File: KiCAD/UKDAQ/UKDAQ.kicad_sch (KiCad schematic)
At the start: 20 parts

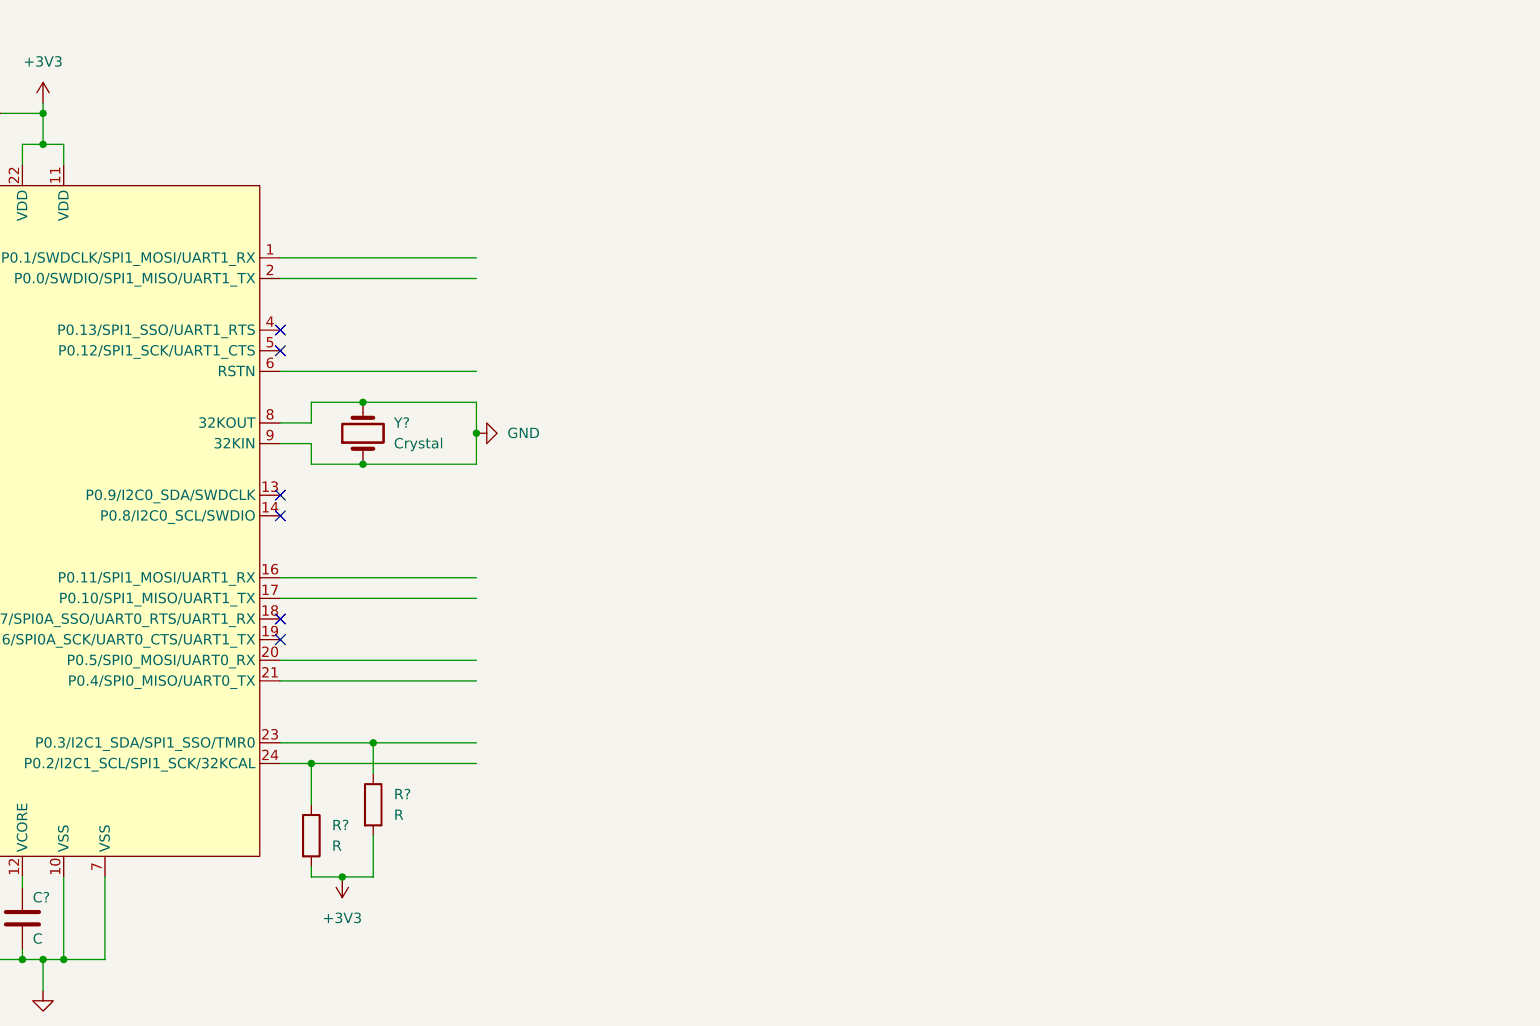
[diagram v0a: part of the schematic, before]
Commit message: created eclipse IDE workspace for dev kit
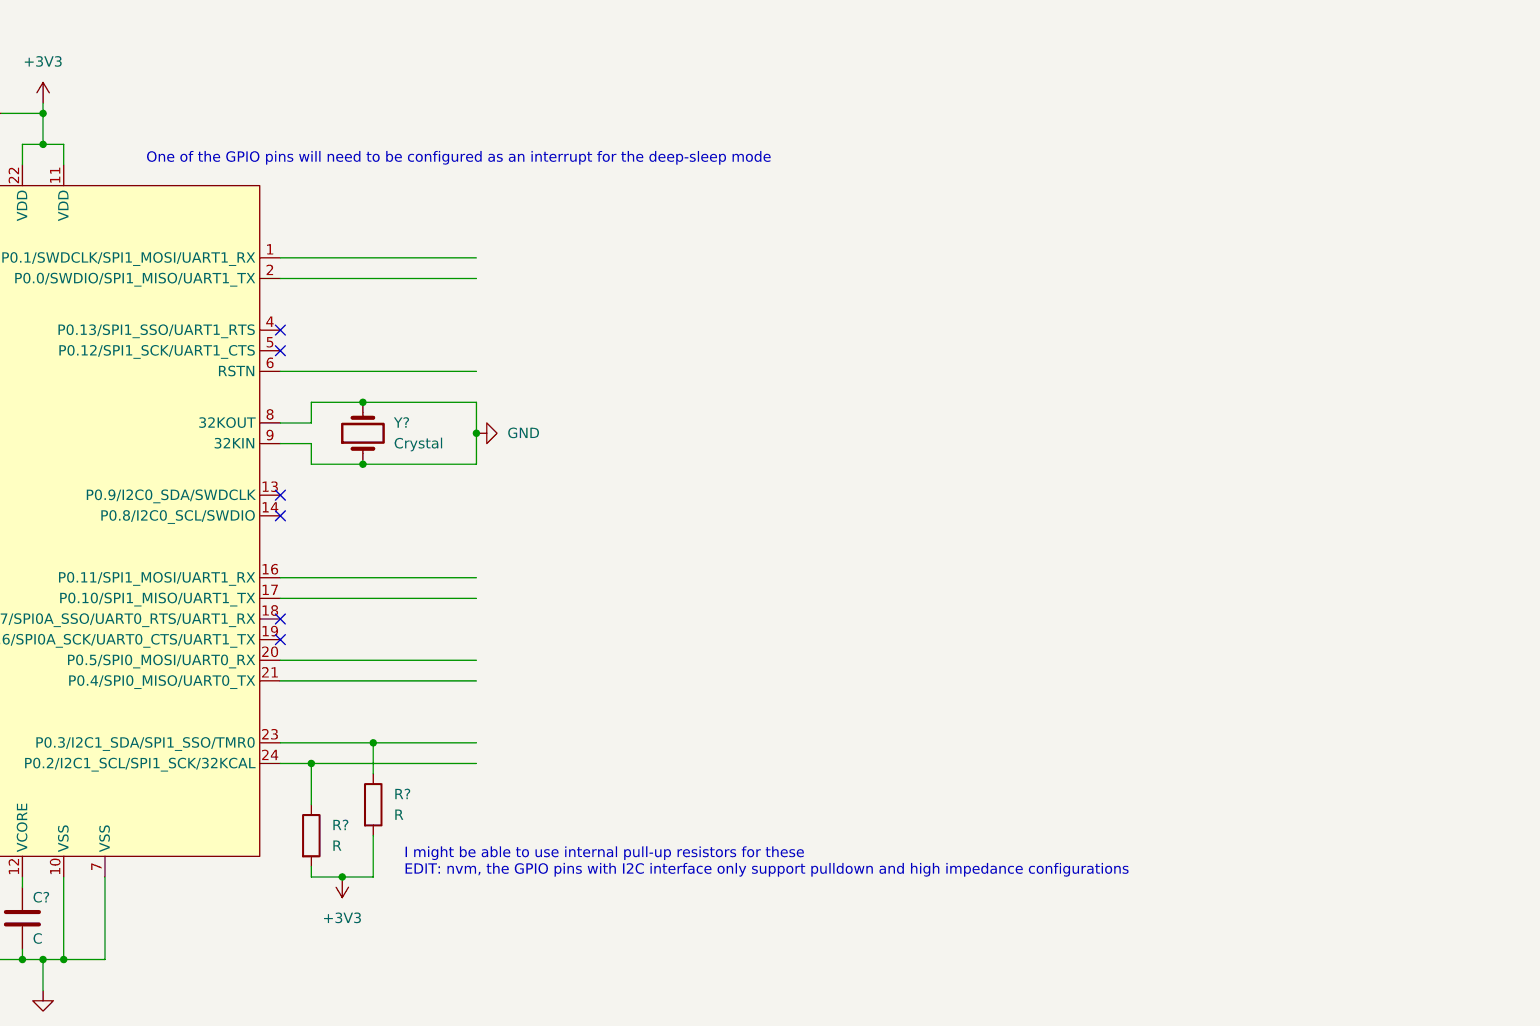
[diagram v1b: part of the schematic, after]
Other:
- note added: "I might be able to use internal pull-up resistors for these EDIT: nvm, the GPIO pins with I2C interface only support pulldown and high impedance configurations"
- note added: "One of the GPIO pins will need to be configured as an interrupt for the deep-sleep mode"
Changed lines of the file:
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@@
     (stroke (width 0) (type default) (color 0 0 0 0))
+  )
+  (text "One of the GPIO pins will need to be configured as an interrupt for the deep-sleep mode"
+    (at 67.31 156.21 0)
+    (effects (font (size 1.27 1.27)) (justify left bottom))
+  )
+  (text "I might be able to use internal pull-up resistors for these\nEDIT: nvm, the GPIO pins with I2C interface only support pulldown and high impedance configurations"
+    (at 99.06 243.84 0)
+    (effects (font (size 1.27 1.27)) (justify left bottom))
   )
   (symbol (lib_id "power:+5V") (at 373.38 212.09 90) (unit 1)

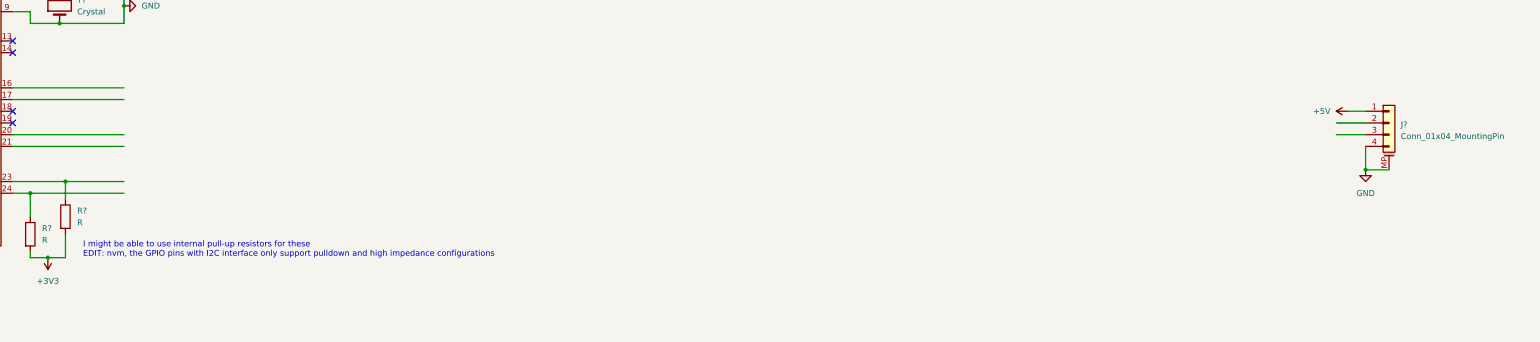
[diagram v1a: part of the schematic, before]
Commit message: data visualization tool
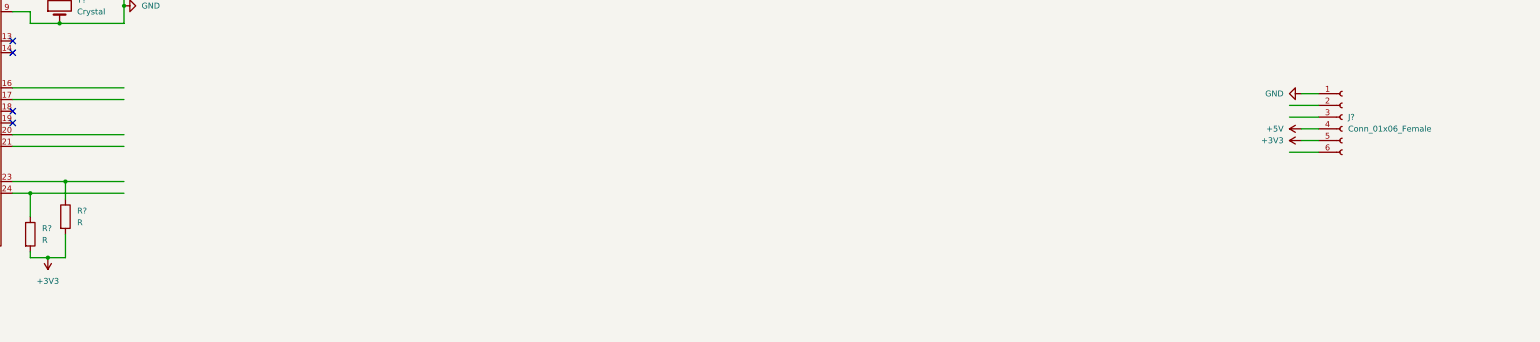
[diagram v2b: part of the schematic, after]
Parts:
- removed J?: Conn_01x04_MountingPin, symbol Connector_Generic_MountingPin:Conn_01x04_MountingPin
- added J?: Conn_01x06_Female, symbol Connector:Conn_01x06_Female
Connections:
- net +3V3: now also J?.5 (Pin_5)
- net +5V: now also J?.4 (Pin_4)
- net GND: now also J?.1 (Pin_1)
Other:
- note removed: "I might be able to use internal pull-up resistors for these EDIT: nvm, the GPIO pins with I2C interface only support pulldown and high impedance configurations"
